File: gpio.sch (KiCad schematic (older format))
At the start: 38 parts, among them J6 Pro Bus, J7 PMOD1, J8 PMOD, SW1 SW_Push, SW2 SW_Push, U15 TXB0108PWR, U16 TXB0108PWR

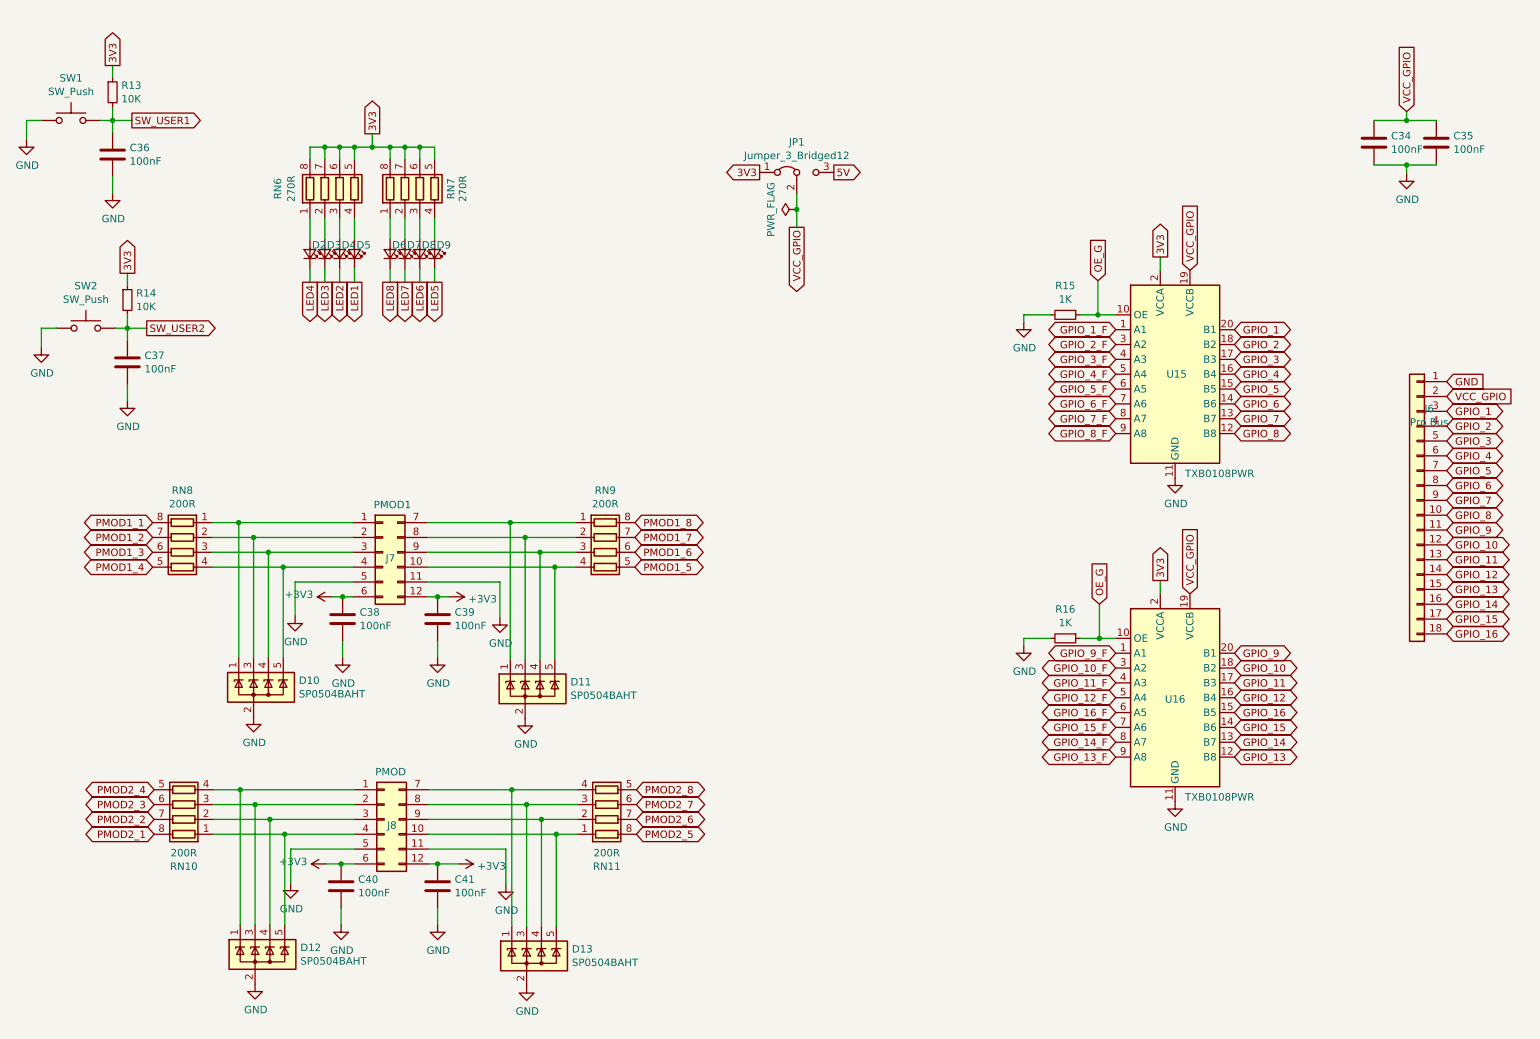
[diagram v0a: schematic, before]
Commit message: moved things around to improve routing, fixed power plane
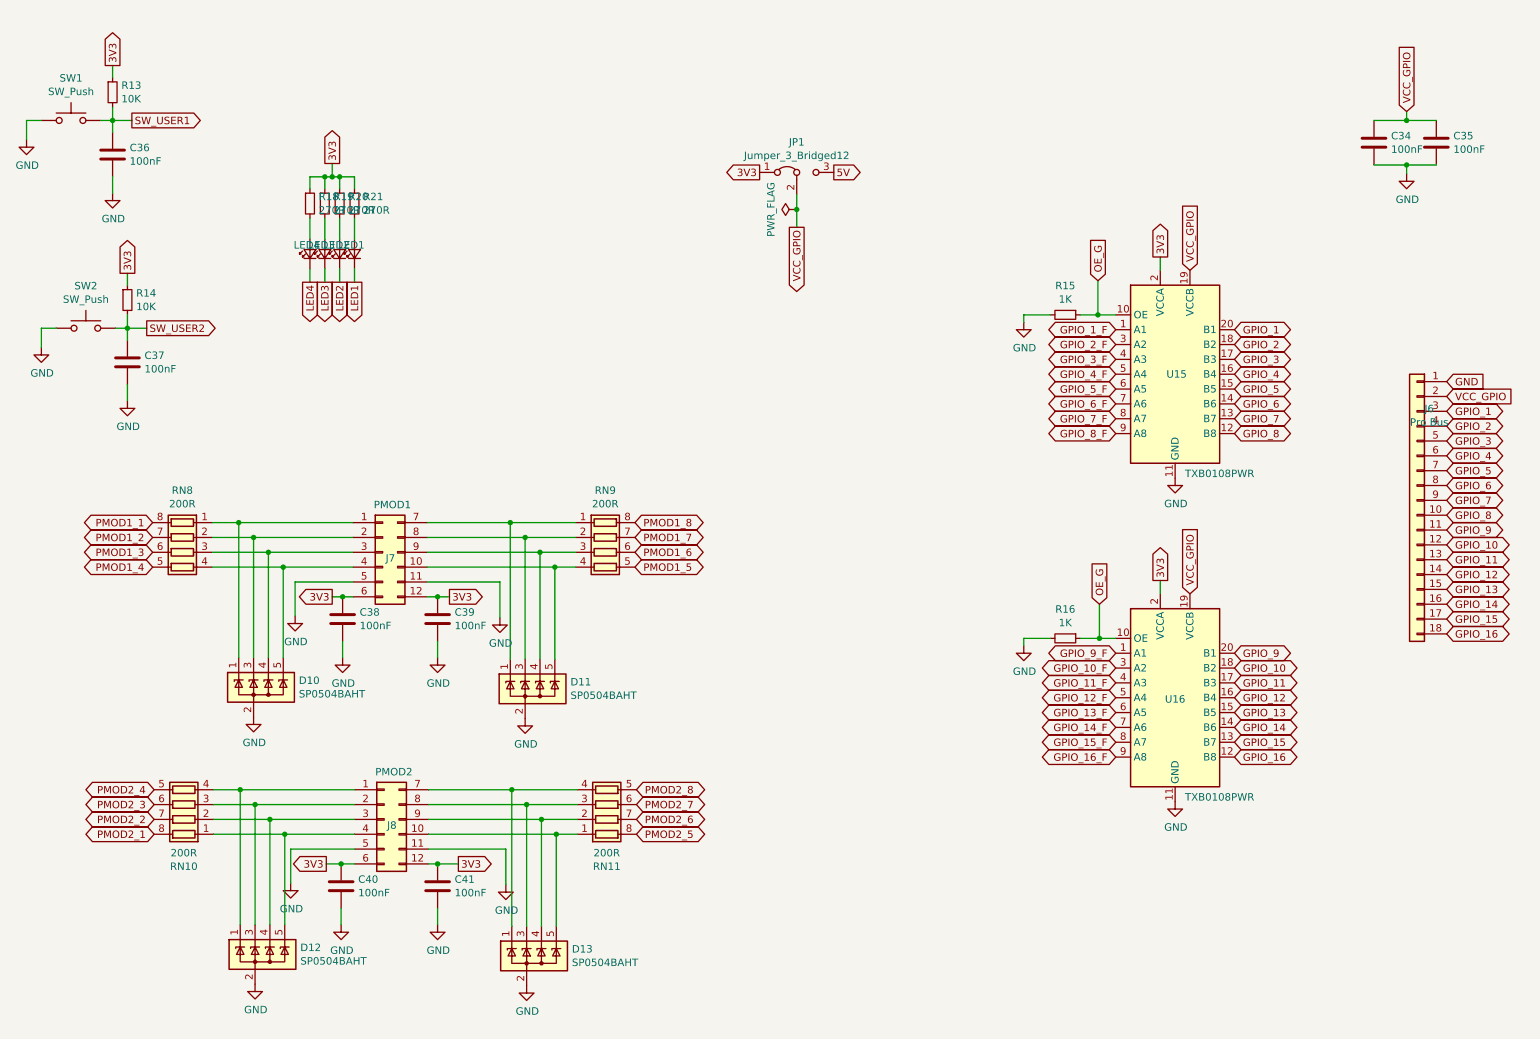
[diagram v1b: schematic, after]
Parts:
- removed D6, D7, D8, D9: Red, LED_SMD:LED_0603_1608Metric_Pad1.05x0.95mm_HandSolder, symbol Device:LED_Small
- removed RN6, RN7: 270R, Resistor_SMD:R_Array_Concave_4x0603, symbol Device:R_Pack04
- added R18, R19, R20, R21: 270R, Resistor_SMD:R_0603_1608Metric_Pad1.05x0.95mm_HandSolder, symbol Device:R_Small
- J8: value PMOD -> PMOD2
- renumbered D2 to LED1, D3 to LED2, D4 to LED3, D5 to LED4
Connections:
- net +3V3 is gone; now on net 3V3: C38.1, C39.1, C40.1, C41.1, J7.12 (Pin_12), J7.6 (Pin_6), J8.12 (Pin_12), J8.6 (Pin_6)
- net 3V3: now also R18.1, R19.1, R20.1, R21.1
- net GPIO_13: now also U16.15 (B5); no longer U16.12 (B8)
- net GPIO_13_F: now also U16.6 (A5); no longer U16.9 (A8)
- net GPIO_14: now also U16.14 (B6); no longer U16.13 (B7)
- net GPIO_14_F: now also U16.7 (A6); no longer U16.8 (A7)
- net GPIO_15: now also U16.13 (B7); no longer U16.14 (B6)
- net GPIO_15_F: now also U16.8 (A7); no longer U16.7 (A6)
- net GPIO_16: now also U16.12 (B8); no longer U16.15 (B5)
- net GPIO_16_F: now also U16.9 (A8); no longer U16.6 (A5)
- net LED1: now also LED1.1 (K); no longer LED4.1 (K)
- net LED2: now also LED2.1 (K); no longer LED3.1 (K)
- net LED3: now also LED3.1 (K); no longer LED2.1 (K)
- net LED4: now also LED4.1 (K); no longer LED1.1 (K)
- net at LED1.2 (A): now also R21.2
- net at LED2.2 (A): now also R20.2
- net at LED3.2 (A): now also R19.2
- net at LED4.2 (A): now also R18.2
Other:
- moved on the sheet: LED1, LED2, LED3, LED4

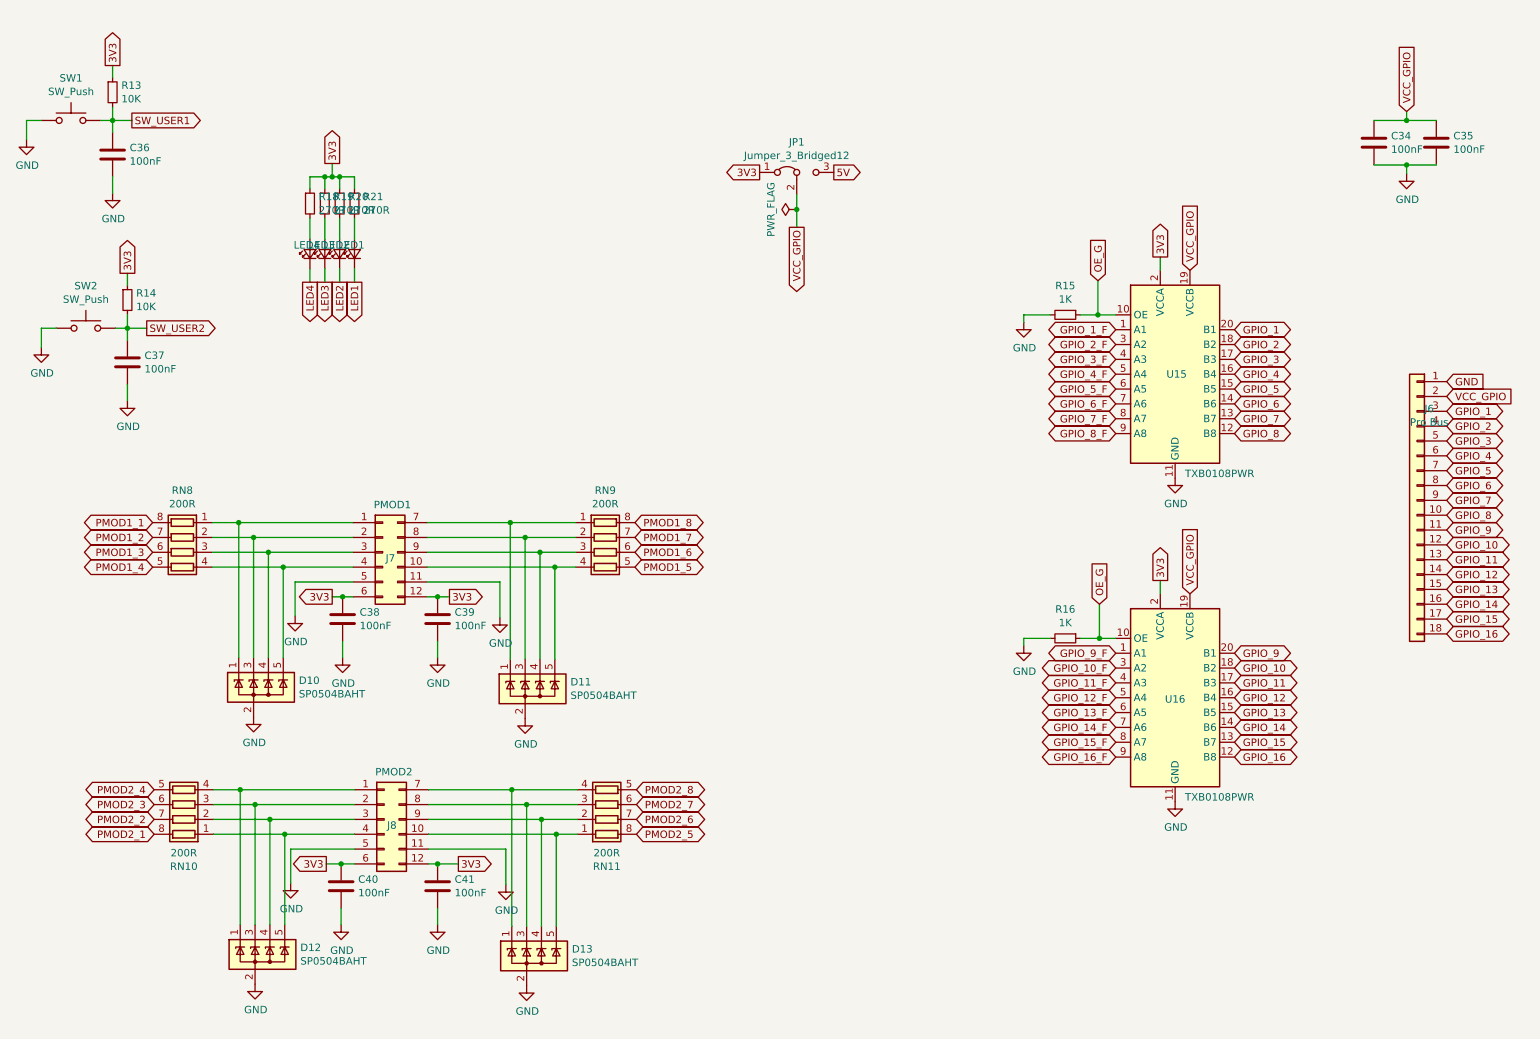
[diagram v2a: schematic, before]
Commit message: Added bus structure, additional pins added, 5V load balancer
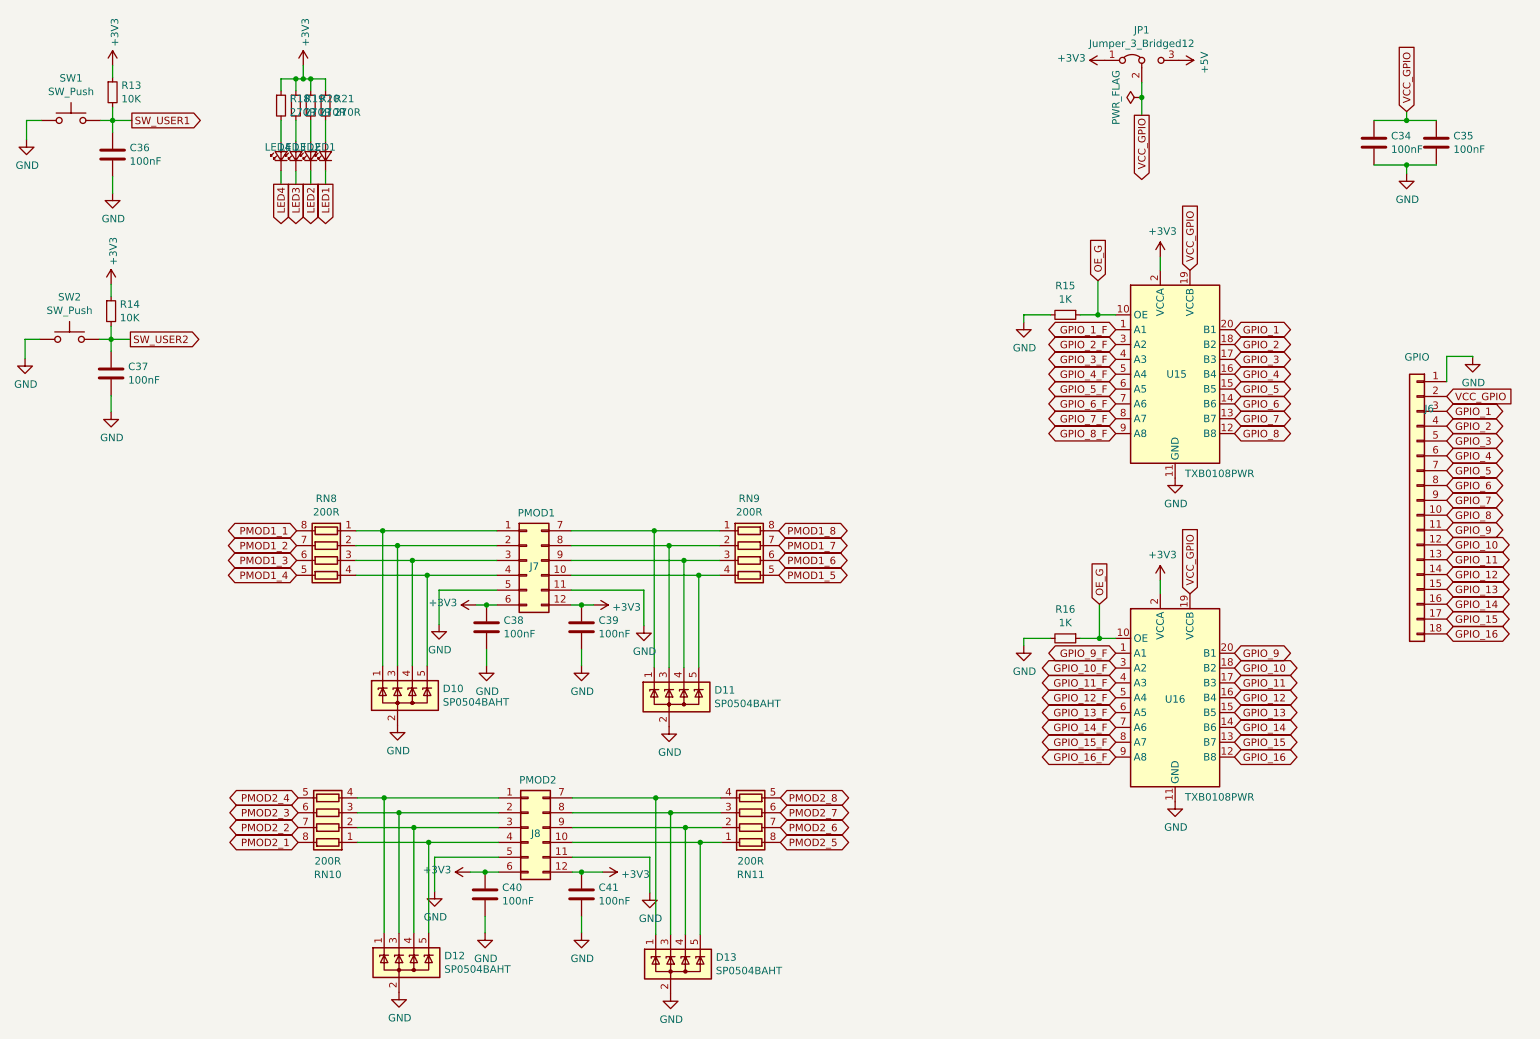
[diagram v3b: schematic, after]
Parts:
- J6: value Pro Bus -> GPIO
- JP1: footprint Connector_PinHeader_2.54mm:PinHeader_1x03_P2.54mm_Vertical -> Connector_PinHeader_2.54mm:PinHeader_1x03_P2.54mm_Horizontal
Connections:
- net 3V3 renamed +3V3
- net 5V renamed +5V
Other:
- moved on the sheet: C37, C38, C39, C40, C41, D10, D11, D12, D13, J7, J8, JP1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
